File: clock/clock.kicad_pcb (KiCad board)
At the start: 2 copper layers, 118 x 118 mm, 4 parts

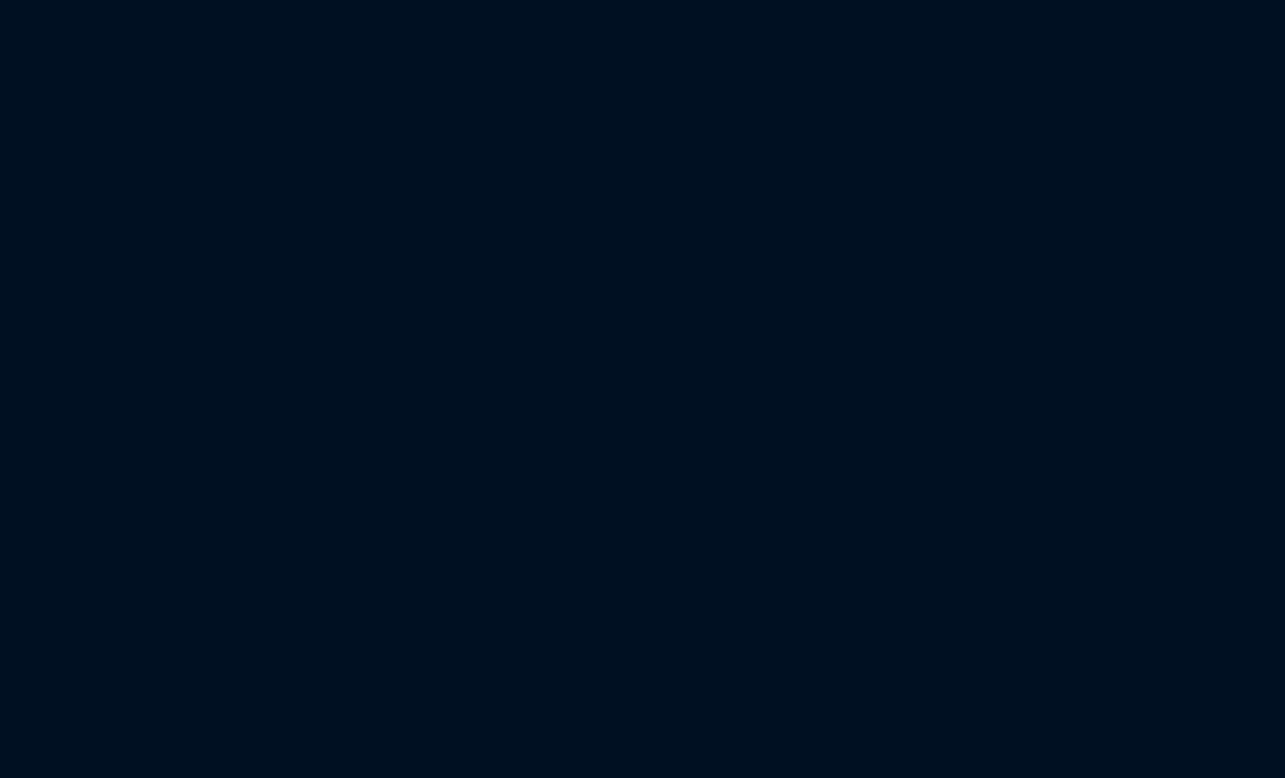
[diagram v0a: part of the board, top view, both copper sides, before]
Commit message: updated clock
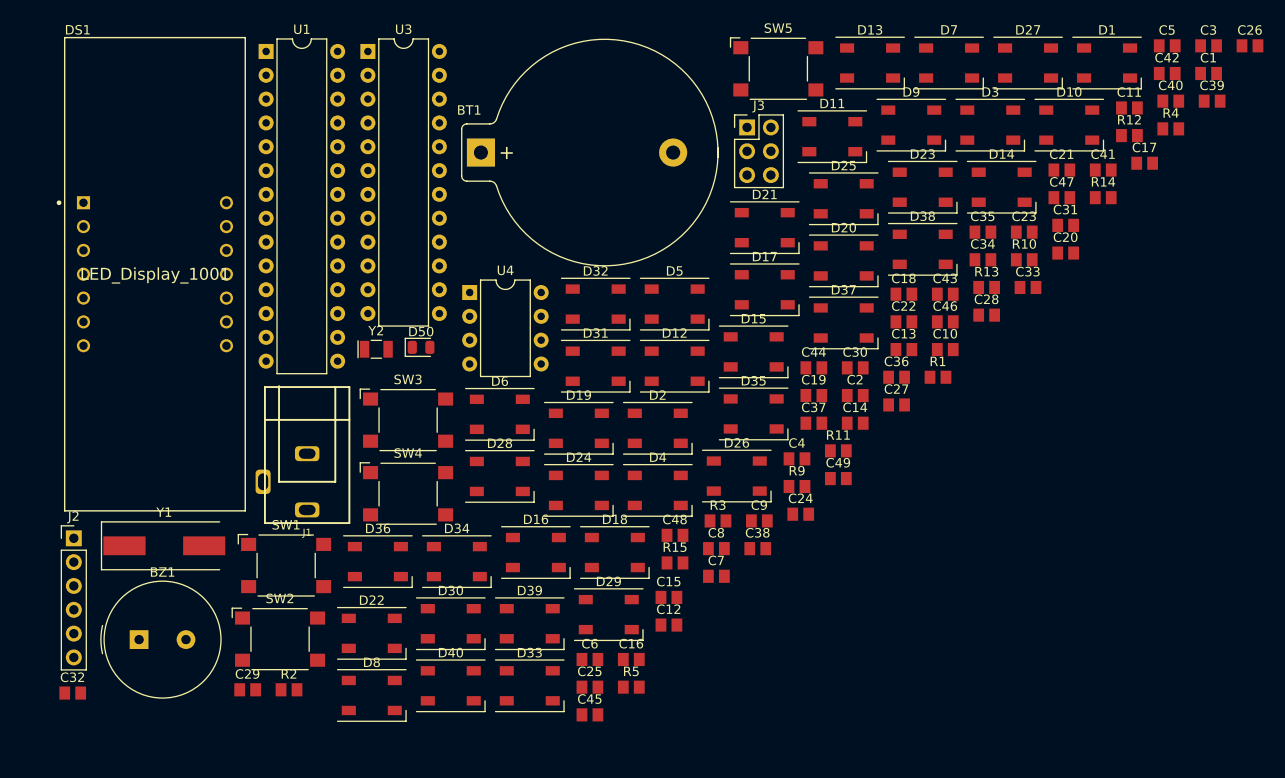
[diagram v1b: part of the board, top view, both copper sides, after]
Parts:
- added BT1: Battery_Cell, footprints:BatteryHolder_Keystone_106_1x20mm, F.Cu at (185.4, -104.1)
- added BZ1: Buzzer, footprints:Buzzer_TDK_PS1240P02BT_D12.2mm_H6.5mm, F.Cu at (149.0, -52.2)
- added C1: 10uf, footprints:C_0805_2012Metric, F.Cu at (263.0, -112.6)
- added C10: 0.1uf, footprints:C_0805_2012Metric, F.Cu at (234.9, -83.1)
- added C11: 0.1uf, footprints:C_0805_2012Metric, F.Cu at (254.6, -108.9)
- added C12: 0.1uf, footprints:C_0805_2012Metric, F.Cu at (205.5, -53.8)
- added C13: 0.1uf, footprints:C_0805_2012Metric, F.Cu at (230.5, -83.1)
- added C14: 0.1uf, footprints:C_0805_2012Metric, F.Cu at (225.3, -75.3)
- added C15: 0.1uf, footprints:C_0805_2012Metric, F.Cu at (205.5, -56.7)
- added C16: 0.1uf, footprints:C_0805_2012Metric, F.Cu at (201.4, -50.1)
- added C17: 0.1uf, footprints:C_0805_2012Metric, F.Cu at (256.2, -103.0)
- added C18: 0.1uf, footprints:C_0805_2012Metric, F.Cu at (230.5, -89.0)
- added C19: 0.1uf, footprints:C_0805_2012Metric, F.Cu at (220.9, -78.2)
- added C2: C_0805_0.1uf, footprints:C_0805_2012Metric, F.Cu at (225.3, -78.2)
- added C20: 0.1uf, footprints:C_0805_2012Metric, F.Cu at (247.8, -93.4)
- added C21: 0.1uf, footprints:C_0805_2012Metric, F.Cu at (247.3, -102.3)
- added C22: 0.1uf, footprints:C_0805_2012Metric, F.Cu at (230.5, -86.1)
- added C23: 0.1uf, footprints:C_0805_2012Metric, F.Cu at (243.3, -95.7)
- added C24: 0.1uf, footprints:C_0805_2012Metric, F.Cu at (219.5, -65.6)
- added C25: 0.1uf, footprints:C_0805_2012Metric, F.Cu at (197.0, -47.1)
- added C26: 0.1uf, footprints:C_0805_2012Metric, F.Cu at (267.4, -115.5)
- added C27: 0.1uf, footprints:C_0805_2012Metric, F.Cu at (229.7, -77.2)
- added C28: 0.1uf, footprints:C_0805_2012Metric, F.Cu at (239.3, -86.8)
- added C29: 0.1uf, footprints:C_0805_2012Metric, F.Cu at (160.6, -46.9)
- added C3: C_0805_0.1uf, footprints:C_0805_2012Metric, F.Cu at (263.0, -115.5)
- added C30: 0.1uf, footprints:C_0805_2012Metric, F.Cu at (225.3, -81.2)
- added C31: 0.1uf, footprints:C_0805_2012Metric, F.Cu at (247.8, -96.4)
- added C32: 0.1uf, footprints:C_0805_2012Metric, F.Cu at (141.9, -46.5)
- added C33: 0.1uf, footprints:C_0805_2012Metric, F.Cu at (243.7, -89.8)
- added C34: 0.1uf, footprints:C_0805_2012Metric, F.Cu at (238.9, -92.7)
- added C35: 0.1uf, footprints:C_0805_2012Metric, F.Cu at (238.9, -95.7)
- added C36: 0.1uf, footprints:C_0805_2012Metric, F.Cu at (229.7, -80.2)
- added C37: 0.1uf, footprints:C_0805_2012Metric, F.Cu at (220.9, -75.3)
- added C38: 0.1uf, footprints:C_0805_2012Metric, F.Cu at (214.9, -61.9)
- added C39: 0.1uf, footprints:C_0805_2012Metric, F.Cu at (263.4, -109.6)
- added C4: 22pf, footprints:C_0805_2012Metric, F.Cu at (219.1, -71.5)
- added C40: 0.1uf, footprints:C_0805_2012Metric, F.Cu at (259.0, -109.6)
- added C41: 0.1uf, footprints:C_0805_2012Metric, F.Cu at (251.8, -102.3)
- added C42: 0.1uf, footprints:C_0805_2012Metric, F.Cu at (258.6, -112.6)
- added C43: 0.1uf, footprints:C_0805_2012Metric, F.Cu at (234.9, -89.0)
- added C44: 0.1uf, footprints:C_0805_2012Metric, F.Cu at (220.9, -81.2)
- added C45: 0.1uf, footprints:C_0805_2012Metric, F.Cu at (197.0, -44.2)
- added C46: 0.1uf, footprints:C_0805_2012Metric, F.Cu at (234.9, -86.1)
- added C47: 0.1uf, footprints:C_0805_2012Metric, F.Cu at (247.3, -99.3)
- added C48: 0.1uf, footprints:C_0805_2012Metric, F.Cu at (206.1, -63.3)
- added C49: 0.1uf, footprints:C_0805_2012Metric, F.Cu at (223.5, -69.4)
- added C5: 22pf, footprints:C_0805_2012Metric, F.Cu at (258.6, -115.5)
- added C6: 1uf, footprints:C_0805_2012Metric, F.Cu at (197.0, -50.1)
- added C7: 0.1uf, footprints:C_0805_2012Metric, F.Cu at (210.5, -59.0)
- added C8: C_0805_0.1uf, footprints:C_0805_2012Metric, F.Cu at (210.5, -61.9)
- added C9: C_0805_10uf, footprints:C_0805_2012Metric, F.Cu at (215.1, -64.9)
- added D1: NEOPIXEL_SMT, footprints:LED_SK6812_PLCC4_5.0x5.0mm_P3.2mm, F.Cu at (252.2, -113.7)
- added D10: NEOPIXEL_SMT, footprints:LED_SK6812_PLCC4_5.0x5.0mm_P3.2mm, F.Cu at (248.1, -107.1)
- added D11: NEOPIXEL_SMT, footprints:LED_SK6812_PLCC4_5.0x5.0mm_P3.2mm, F.Cu at (222.9, -105.8)
- added D12: NEOPIXEL_SMT, footprints:LED_SK6812_PLCC4_5.0x5.0mm_P3.2mm, F.Cu at (206.1, -81.4)
- added D13: NEOPIXEL_SMT, footprints:LED_SK6812_PLCC4_5.0x5.0mm_P3.2mm, F.Cu at (226.9, -113.7)
- added D14: NEOPIXEL_SMT, footprints:LED_SK6812_PLCC4_5.0x5.0mm_P3.2mm, F.Cu at (240.9, -100.4)
- added D15: NEOPIXEL_SMT, footprints:LED_SK6812_PLCC4_5.0x5.0mm_P3.2mm, F.Cu at (214.5, -82.9)
- added D16: NEOPIXEL_SMT, footprints:LED_SK6812_PLCC4_5.0x5.0mm_P3.2mm, F.Cu at (191.3, -61.5)
- added D17: NEOPIXEL_SMT, footprints:LED_SK6812_PLCC4_5.0x5.0mm_P3.2mm, F.Cu at (215.7, -89.5)
- added D18: NEOPIXEL_SMT, footprints:LED_SK6812_PLCC4_5.0x5.0mm_P3.2mm, F.Cu at (199.7, -61.5)
- added D19: NEOPIXEL_SMT, footprints:LED_SK6812_PLCC4_5.0x5.0mm_P3.2mm, F.Cu at (195.9, -74.7)
- added D2: NEOPIXEL_SMT, footprints:LED_SK6812_PLCC4_5.0x5.0mm_P3.2mm, F.Cu at (204.3, -74.7)
- added D20: NEOPIXEL_SMT, footprints:LED_SK6812_PLCC4_5.0x5.0mm_P3.2mm, F.Cu at (224.1, -92.6)
- added D21: NEOPIXEL_SMT, footprints:LED_SK6812_PLCC4_5.0x5.0mm_P3.2mm, F.Cu at (215.7, -96.1)
- added D22: NEOPIXEL_SMT, footprints:LED_SK6812_PLCC4_5.0x5.0mm_P3.2mm, F.Cu at (173.8, -52.9)
- added D23: NEOPIXEL_SMT, footprints:LED_SK6812_PLCC4_5.0x5.0mm_P3.2mm, F.Cu at (232.5, -100.4)
- added D24: NEOPIXEL_SMT, footprints:LED_SK6812_PLCC4_5.0x5.0mm_P3.2mm, F.Cu at (195.9, -68.1)
- added D25: NEOPIXEL_SMT, footprints:LED_SK6812_PLCC4_5.0x5.0mm_P3.2mm, F.Cu at (224.1, -99.2)
- added D26: NEOPIXEL_SMT, footprints:LED_SK6812_PLCC4_5.0x5.0mm_P3.2mm, F.Cu at (212.7, -69.7)
- added D27: NEOPIXEL_SMT, footprints:LED_SK6812_PLCC4_5.0x5.0mm_P3.2mm, F.Cu at (243.7, -113.7)
- added D28: NEOPIXEL_SMT, footprints:LED_SK6812_PLCC4_5.0x5.0mm_P3.2mm, F.Cu at (187.4, -69.6)
- added D29: NEOPIXEL_SMT, footprints:LED_SK6812_PLCC4_5.0x5.0mm_P3.2mm, F.Cu at (199.0, -54.9)
- added D3: NEOPIXEL_SMT, footprints:LED_SK6812_PLCC4_5.0x5.0mm_P3.2mm, F.Cu at (239.7, -107.1)
- added D30: NEOPIXEL_SMT, footprints:LED_SK6812_PLCC4_5.0x5.0mm_P3.2mm, F.Cu at (182.2, -53.9)
- added D31: NEOPIXEL_SMT, footprints:LED_SK6812_PLCC4_5.0x5.0mm_P3.2mm, F.Cu at (197.7, -81.4)
- added D32: NEOPIXEL_SMT, footprints:LED_SK6812_PLCC4_5.0x5.0mm_P3.2mm, F.Cu at (197.7, -88.0)
- added D33: NEOPIXEL_SMT, footprints:LED_SK6812_PLCC4_5.0x5.0mm_P3.2mm, F.Cu at (190.6, -47.3)
- added D34: NEOPIXEL_SMT, footprints:LED_SK6812_PLCC4_5.0x5.0mm_P3.2mm, F.Cu at (182.9, -60.5)
- added D35: NEOPIXEL_SMT, footprints:LED_SK6812_PLCC4_5.0x5.0mm_P3.2mm, F.Cu at (214.5, -76.3)
- added D36: NEOPIXEL_SMT, footprints:LED_SK6812_PLCC4_5.0x5.0mm_P3.2mm, F.Cu at (174.4, -60.5)
- added D37: NEOPIXEL_SMT, footprints:LED_SK6812_PLCC4_5.0x5.0mm_P3.2mm, F.Cu at (224.1, -86.0)
- added D38: NEOPIXEL_SMT, footprints:LED_SK6812_PLCC4_5.0x5.0mm_P3.2mm, F.Cu at (232.5, -93.8)
- added D39: NEOPIXEL_SMT, footprints:LED_SK6812_PLCC4_5.0x5.0mm_P3.2mm, F.Cu at (190.6, -53.9)
- added D4: NEOPIXEL_SMT, footprints:LED_SK6812_PLCC4_5.0x5.0mm_P3.2mm, F.Cu at (204.3, -68.1)
- added D40: NEOPIXEL_SMT, footprints:LED_SK6812_PLCC4_5.0x5.0mm_P3.2mm, F.Cu at (182.2, -47.3)
- added D5: NEOPIXEL_SMT, footprints:LED_SK6812_PLCC4_5.0x5.0mm_P3.2mm, F.Cu at (206.1, -88.0)
- added D50: LED_0805, footprints:LED_0805_2012Metric, F.Cu at (179.0, -83.4)
- added D6: NEOPIXEL_SMT, footprints:LED_SK6812_PLCC4_5.0x5.0mm_P3.2mm, F.Cu at (187.4, -76.2)
- added D7: NEOPIXEL_SMT, footprints:LED_SK6812_PLCC4_5.0x5.0mm_P3.2mm, F.Cu at (235.3, -113.7)
- added D8: NEOPIXEL_SMT, footprints:LED_SK6812_PLCC4_5.0x5.0mm_P3.2mm, F.Cu at (173.8, -46.3)
- added D9: NEOPIXEL_SMT, footprints:LED_SK6812_PLCC4_5.0x5.0mm_P3.2mm, F.Cu at (231.3, -107.1)
- added DS1: LED_Display_1001, footprints:Adafruit-1001-0-0-MFG, F.Cu at (150.7, -91.2)
- added J1: PJ-102AH, footprints:PJ-102AH, F.Cu at (166.9, -69.0)
- added J2: Conn_01x06, footprints:PinHeader_1x06_P2.54mm_Vertical, F.Cu at (142.0, -63.0)
- added J3: Conn_02x03_Odd_Even, footprints:PinHeader_2x03_P2.54mm_Vertical, F.Cu at (213.8, -106.8)
- added R1: 2.2K, footprints:R_0805_2012Metric, F.Cu at (234.1, -80.2)
- added R10: R_0805_10K, footprints:R_0805_2012Metric, F.Cu at (243.3, -92.7)
- added R11: R_0805_10K, footprints:R_0805_2012Metric, F.Cu at (223.5, -72.3)
- added R12: R_0805_10K, footprints:R_0805_2012Metric, F.Cu at (254.6, -105.9)
- added R13: R_0805_47, footprints:R_0805_2012Metric, F.Cu at (239.3, -89.8)
- added R14: 4.7K, footprints:R_0805_2012Metric, F.Cu at (251.8, -99.3)
- added R15: 4.7K, footprints:R_0805_2012Metric, F.Cu at (206.1, -60.4)
- added R2: 10K, footprints:R_0805_2012Metric, F.Cu at (165.0, -46.9)
- added R3: 47, footprints:R_0805_2012Metric, F.Cu at (210.7, -64.9)
- added R4: 47, footprints:R_0805_2012Metric, F.Cu at (259.0, -106.7)
- added R5: R_0805_22K, footprints:R_0805_2012Metric, F.Cu at (201.4, -47.1)
- added R9: R_0805_10K, footprints:R_0805_2012Metric, F.Cu at (219.1, -68.5)
- added SW1: Omron_B3F_SPST, footprints:SW_SPST_Omron_B3FS-100xP, F.Cu at (164.7, -60.1)
- added SW2: Omron_B3F_SPST, footprints:SW_SPST_Omron_B3FS-100xP, F.Cu at (164.0, -52.3)
- added SW3: Omron_B3F_SPST, footprints:SW_SPST_Omron_B3FS-100xP, F.Cu at (177.7, -75.6)
- added SW4: Omron_B3F_SPST, footprints:SW_SPST_Omron_B3FS-100xP, F.Cu at (177.7, -67.8)
- added SW5: Omron_B3F_SPST, footprints:SW_SPST_Omron_B3FS-100xP, F.Cu at (217.1, -113.1)
- added U1: ATmega328-PU, footprints:DIP-28_W7.62mm, F.Cu at (162.5, -114.9)
- added U3: MAX7219, footprints:DIP-24_W7.62mm, F.Cu at (173.4, -114.9)
- added U4: DS1307_DIP-8, footprints:DIP-8_W7.62mm, F.Cu at (184.2, -89.2)
- added Y1: 16MHz, footprints:Crystal_SMD_HC49-SD, F.Cu at (151.7, -62.2)
- added Y2: Crystal_32768Hz, footprints:Crystal_SMD_2Pin_3.2x1.5mm, F.Cu at (174.3, -83.2)
